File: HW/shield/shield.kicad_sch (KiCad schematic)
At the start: 78 parts, among them J1 TRG, J2 E-STOP, J3 UART, J4 IO, J5 LDP-C BOB, J6 VIN, J7 BREAK, Q1 BSS138, Q2 BSS138, Q3 BSS138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

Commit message: PCB layout
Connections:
- net SCL: now also A1.13 (SDA/A4)
- net SDA: now also A1.14 (SCL/A5)
- no-connect marks 10 -> 8
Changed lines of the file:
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@@
   (junction (at 40.005 72.39) (diameter 0) (color 0 0 0 0)
   )
+  (junction (at 115.57 66.04) (diameter 0) (color 0 0 0 0)
+  )
   (junction (at 38.1 48.26) (diameter 0) (color 0 0 0 0)
   )
@@
   )
   (junction (at 76.2 81.28) (diameter 0) (color 0 0 0 0)
+  )
+  (junction (at 116.205 63.5) (diameter 0) (color 0 0 0 0)
   )
   (no_connect (at 114.935 30.48))
   (no_connect (at 99.695 20.32))
-  (no_connect (at 114.935 55.88))
-  (no_connect (at 114.935 58.42))
   (no_connect (at 44.45 132.08))
   (no_connect (at 114.935 35.56))
@@
     (stroke (width 0) (type default) (color 0 0 0 0))
   )
+  (wire (pts (xy 116.205 63.5) (xy 121.92 63.5))
+    (stroke (width 0) (type default) (color 0 0 0 0))
+  )
   (wire (pts (xy 165.735 66.04) (xy 176.53 66.04))
     (stroke (width 0) (type default) (color 0 0 0 0))
@@
     (stroke (width 0) (type default) (color 0 0 0 0))
   )
+  (wire (pts (xy 115.57 66.04) (xy 133.985 66.04))
+    (stroke (width 0) (type default) (color 0 0 0 0))
+  )
   (wire (pts (xy 165.1 135.255) (xy 156.845 135.255))
     (stroke (width 0) (type default) (color 0 0 0 0))
@@
     (stroke (width 0) (type default) (color 0 0 0 0))
   )
+  (wire (pts (xy 114.935 55.88) (xy 116.205 55.88))
+    (stroke (width 0) (type default) (color 0 0 0 0))
+  )
   (wire (pts (xy 250.19 50.8) (xy 250.19 44.45))
     (stroke (width 0) (type default) (color 0 0 0 0))
@@
     (stroke (width 0) (type default) (color 0 0 0 0))
   )
-  (wire (pts (xy 114.935 66.04) (xy 133.985 66.04))
+  (wire (pts (xy 114.935 66.04) (xy 115.57 66.04))
     (stroke (width 0) (type default) (color 0 0 0 0))
   )
@@
     (stroke (width 0) (type default) (color 0 0 0 0))
   )
-  (wire (pts (xy 114.935 63.5) (xy 121.92 63.5))
+  (wire (pts (xy 114.935 63.5) (xy 116.205 63.5))
     (stroke (width 0) (type default) (color 0 0 0 0))
   )
@@
     (stroke (width 0) (type default) (color 0 0 0 0))
   )
+  (wire (pts (xy 115.57 58.42) (xy 115.57 66.04))
+    (stroke (width 0) (type default) (color 0 0 0 0))
+  )
   (wire (pts (xy 40.005 64.135) (xy 40.005 72.39))
     (stroke (width 0) (type default) (color 0 0 0 0))
@@
     (stroke (width 0) (type default) (color 0 0 0 0))
   )
+  (wire (pts (xy 114.935 58.42) (xy 115.57 58.42))
+    (stroke (width 0) (type default) (color 0 0 0 0))
+  )
   (wire (pts (xy 260.35 36.83) (xy 269.875 36.83))
     (stroke (width 0) (type default) (color 0 0 0 0))
@@
     (stroke (width 0) (type default) (color 0 0 0 0))
   )
+  (wire (pts (xy 116.205 55.88) (xy 116.205 63.5))
+    (stroke (width 0) (type default) (color 0 0 0 0))
+  )

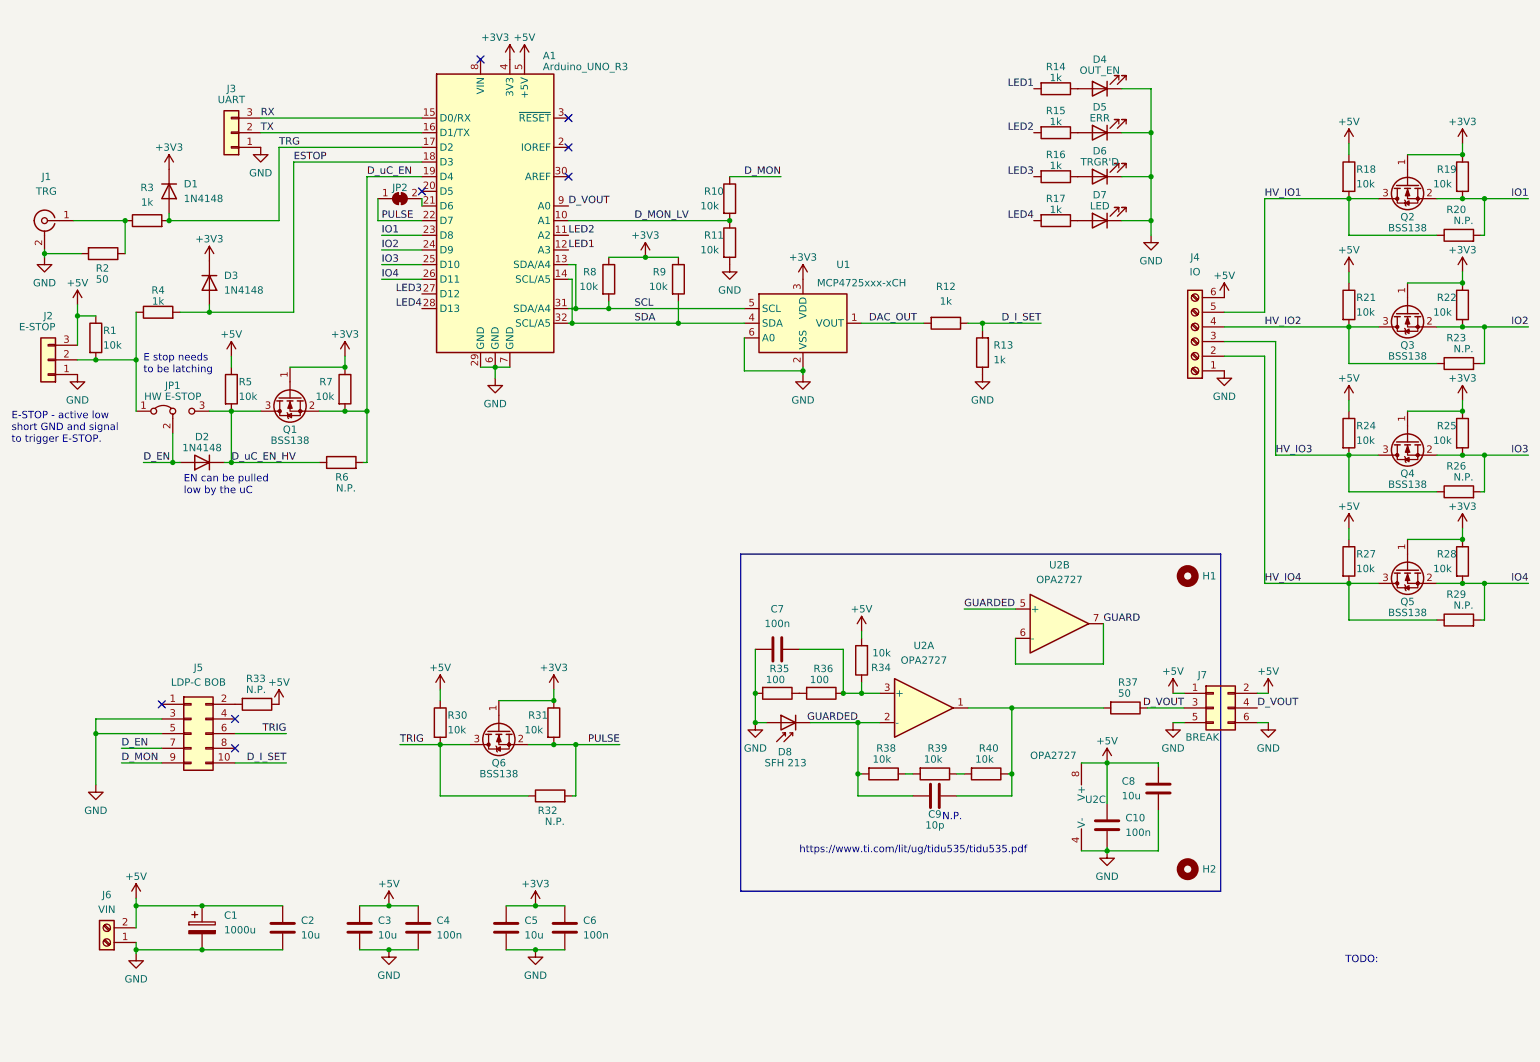
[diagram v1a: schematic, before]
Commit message: PCB routing finished, needs checking
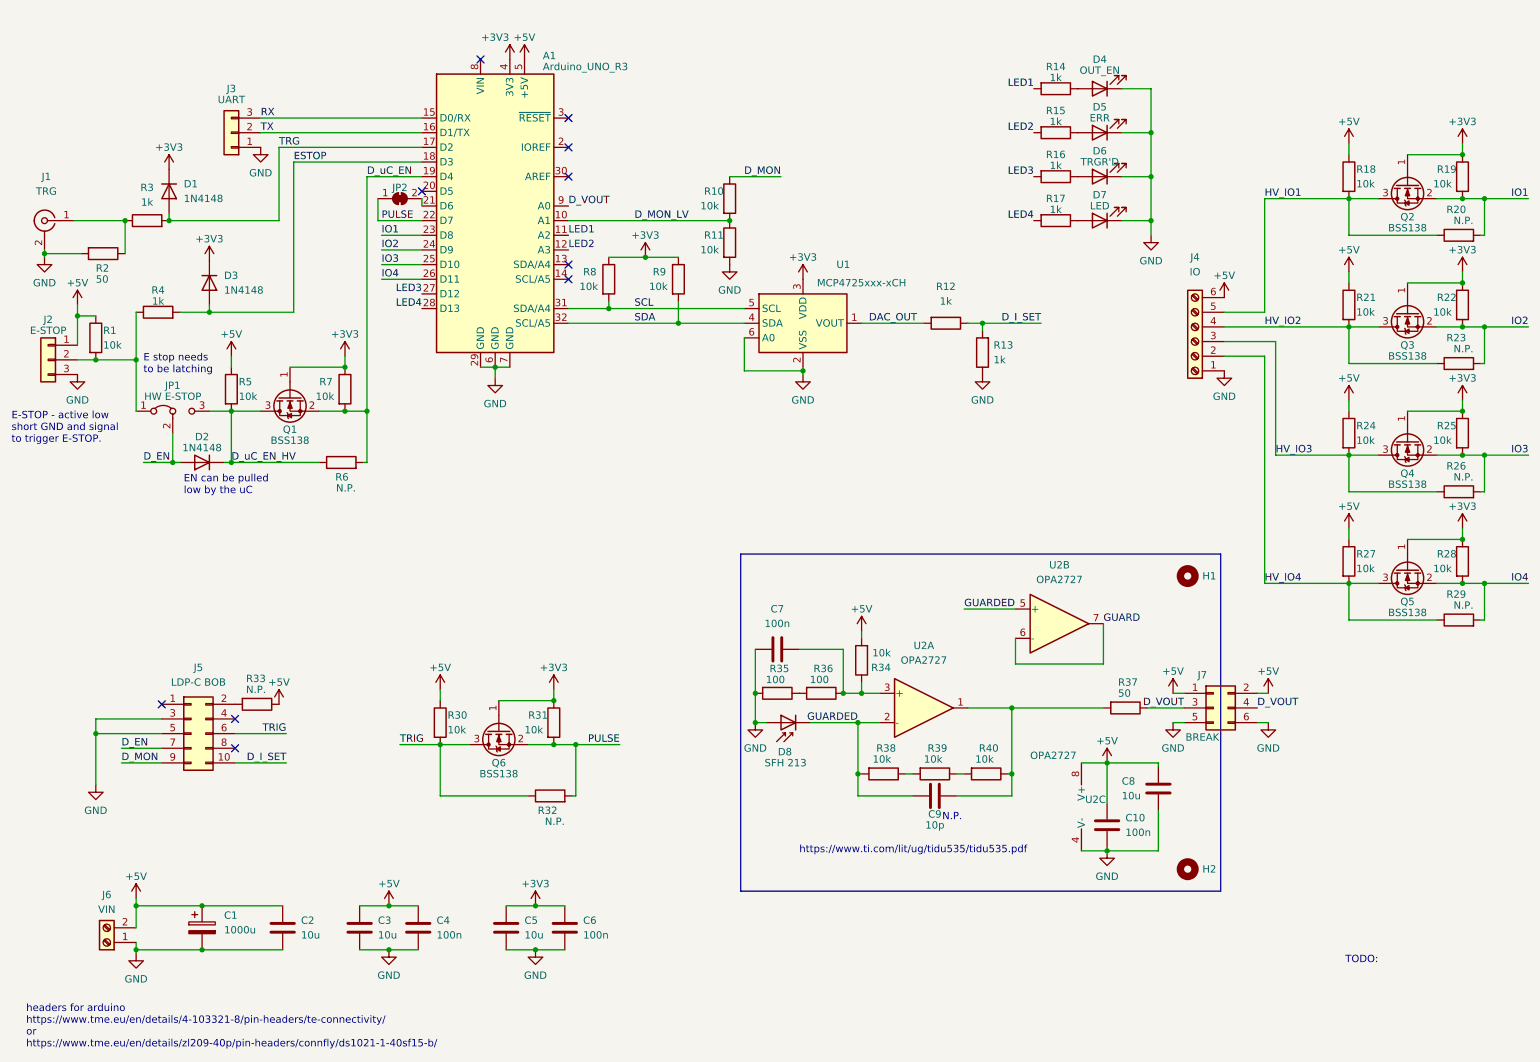
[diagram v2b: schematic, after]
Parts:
- JP2: footprint Jumper:SolderJumper-2_P1.3mm_Open_RoundedPad1.0x1.5mm -> Jumper:SolderJumper-2_P1.3mm_Bridged2Bar_RoundedPad1.0x1.5mm
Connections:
- net +5V: now also J2.1 (Pin_1); no longer J2.3 (Pin_3)
- net GND: now also J2.3 (Pin_3); no longer J2.1 (Pin_1)
- net LED1: now also A1.11 (A2); no longer A1.12 (A3)
- net LED2: now also A1.12 (A3); no longer A1.11 (A2)
- net SCL: no longer A1.13 (SDA/A4)
- net SDA: no longer A1.14 (SCL/A5)
- no-connect marks 8 -> 10
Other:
- note added: "headers for arduino https://www.tme.eu/en/details/4-103321-8/pin-headers/te-connectivity/ or https://www.tme.eu/en/details/zl209-40p/pin-headers/connfly/ds1021-1-40sf15-b/"
- moved on the sheet: J2
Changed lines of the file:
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@@
   (junction (at 40.005 72.39) (diameter 0) (color 0 0 0 0)
   )
-  (junction (at 115.57 66.04) (diameter 0) (color 0 0 0 0)
-  )
   (junction (at 38.1 48.26) (diameter 0) (color 0 0 0 0)
   )
@@
   (junction (at 76.2 81.28) (diameter 0) (color 0 0 0 0)
   )
-  (junction (at 116.205 63.5) (diameter 0) (color 0 0 0 0)
-  )
   (no_connect (at 114.935 30.48))
   (no_connect (at 99.695 20.32))
@@
   (no_connect (at 114.935 40.64))
   (no_connect (at 89.535 43.18))
+  (no_connect (at 114.935 55.88))
   (no_connect (at 57.15 139.7))
   (no_connect (at 57.15 134.62))
+  (no_connect (at 114.935 58.42))
   (wire (pts (xy 51.435 167.005) (xy 65.405 167.005))
     (stroke (width 0) (type default) (color 0 0 0 0))
@@
     (stroke (width 0) (type default) (color 0 0 0 0))
   )
-  (wire (pts (xy 116.205 63.5) (xy 121.92 63.5))
+  (wire (pts (xy 114.935 63.5) (xy 121.92 63.5))
     (stroke (width 0) (type default) (color 0 0 0 0))
   )
@@
     (stroke (width 0) (type default) (color 0 0 0 0))
   )
-  (wire (pts (xy 115.57 66.04) (xy 133.985 66.04))
+  (wire (pts (xy 114.935 66.04) (xy 133.985 66.04))
     (stroke (width 0) (type default) (color 0 0 0 0))
   )
@@
     (stroke (width 0) (type default) (color 0 0 0 0))
   )
-  (wire (pts (xy 114.935 55.88) (xy 116.205 55.88))
-    (stroke (width 0) (type default) (color 0 0 0 0))
-  )
   (wire (pts (xy 250.19 50.8) (xy 250.19 44.45))
     (stroke (width 0) (type default) (color 0 0 0 0))
@@
     (stroke (width 0) (type default) (color 0 0 0 0))
   )
-  (wire (pts (xy 114.935 66.04) (xy 115.57 66.04))
-    (stroke (width 0) (type default) (color 0 0 0 0))
-  )
   (wire (pts (xy 66.675 73.66) (xy 76.2 73.66))
     (stroke (width 0) (type default) (color 0 0 0 0))
@@
     (stroke (width 0) (type default) (color 0 0 0 0))
   )
-  (wire (pts (xy 114.935 63.5) (xy 116.205 63.5))
-    (stroke (width 0) (type default) (color 0 0 0 0))
-  )
   (wire (pts (xy 52.705 62.865) (xy 52.705 64.135))
     (stroke (width 0) (type default) (color 0 0 0 0))
@@
     (stroke (width 0) (type default) (color 0 0 0 0))
   )
-  (wire (pts (xy 115.57 58.42) (xy 115.57 66.04))
-    (stroke (width 0) (type default) (color 0 0 0 0))
-  )
   (wire (pts (xy 40.005 64.135) (xy 40.005 72.39))
     (stroke (width 0) (type default) (color 0 0 0 0))
@@
     (stroke (width 0) (type default) (color 0 0 0 0))
   )
-  (wire (pts (xy 114.935 58.42) (xy 115.57 58.42))
-    (stroke (width 0) (type default) (color 0 0 0 0))
-  )
   (wire (pts (xy 260.35 36.83) (xy 269.875 36.83))
     (stroke (width 0) (type default) (color 0 0 0 0))
@@
     (stroke (width 0) (type default) (color 0 0 0 0))
   )
-  (wire (pts (xy 116.205 55.88) (xy 116.205 63.5))
-    (stroke (width 0) (type default) (color 0 0 0 0))
-  )
   (wire (pts (xy 92.71 129.54) (xy 92.71 131.445))
     (stroke (width 0) (type default) (color 0 0 0 0))
@@
     (effects (font (size 1.27 1.27)) (justify left bottom))
   )
+  (text "headers for arduino\nhttps://www.tme.eu/en/details/4-103321-8/pin-headers/te-connectivity/\nor\nhttps://www.tme.eu/en/details/zl209-40p/pin-headers/connfly/ds1021-1-40sf15-b/"
+    (at 20.955 191.77 0)
+    (effects (font (size 1.27 1.27)) (justify left bottom))
+  )
   (text "N.P." (at 179.705 152.4 0)
     (effects (font (size 1.27 1.27)) (justify left bottom))
@@
     (effects (font (size 1.27 1.27)) (justify left bottom))
   )
-  (label "LED1" (at 114.935 53.34 0)
+  (label "LED1" (at 114.935 50.8 0)
     (effects (font (size 1.27 1.27)) (justify left bottom))
   )
@@
     (effects (font (size 1.27 1.27)) (justify left bottom))
   )
-  (label "LED2" (at 114.935 50.8 0)
+  (label "LED2" (at 114.935 53.34 0)
     (effects (font (size 1.27 1.27)) (justify left bottom))
   )
@@
     (pin "2")
   )
-  (symbol (lib_id "Connector_Generic:Conn_01x03") (at 24.765 72.39 180) (unit 1)
+  (symbol (lib_id "Connector_Generic:Conn_01x03") (at 24.765 72.39 0) (mirror y) (unit 1)
     (in_bom yes) (on_board yes)
-    (property "Reference" "J2" (id 0) (at 24.765 64.77 0))
-    (property "Value" "E-STOP" (id 1) (at 22.86 66.675 0))
+    (property "Reference" "J2" (id 0) (at 24.765 65.405 0))
+    (property "Value" "E-STOP" (id 1) (at 24.765 67.31 0))
     (property "Footprint" "TerminalBlock:TerminalBlock_Altech_AK300-3_P5.00mm" (id 2) (at 24.765 72.39 0)
       (effects (font (size 1.27 1.27)) hide)
@@
       (effects (font (size 1.27 1.27)) hide)
     )
-    (property "Footprint" "Jumper:SolderJumper-2_P1.3mm_Open_RoundedPad1.0x1.5mm" (id 2) (at 85.725 44.45 0)
+    (property "Footprint" "Jumper:SolderJumper-2_P1.3mm_Bridged2Bar_RoundedPad1.0x1.5mm" (id 2) (at 85.725 44.45 0)
       (effects (font (size 1.27 1.27)) hide)
     )
@@
     )
     (path "/69e4916a-fcd5-499c-859e-5b7a7ee48695"
-      (reference "JP2") (unit 1) (value "INTR") (footprint "Jumper:SolderJumper-2_P1.3mm_Open_RoundedPad1.0x1.5mm")
+      (reference "JP2") (unit 1) (value "INTR") (footprint "Jumper:SolderJumper-2_P1.3mm_Bridged2Bar_RoundedPad1.0x1.5mm")
     )
     (path "/6a7a0bfa-65c7-4518-a3bd-a77ff7b676a3"

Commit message: added LDO, BOM
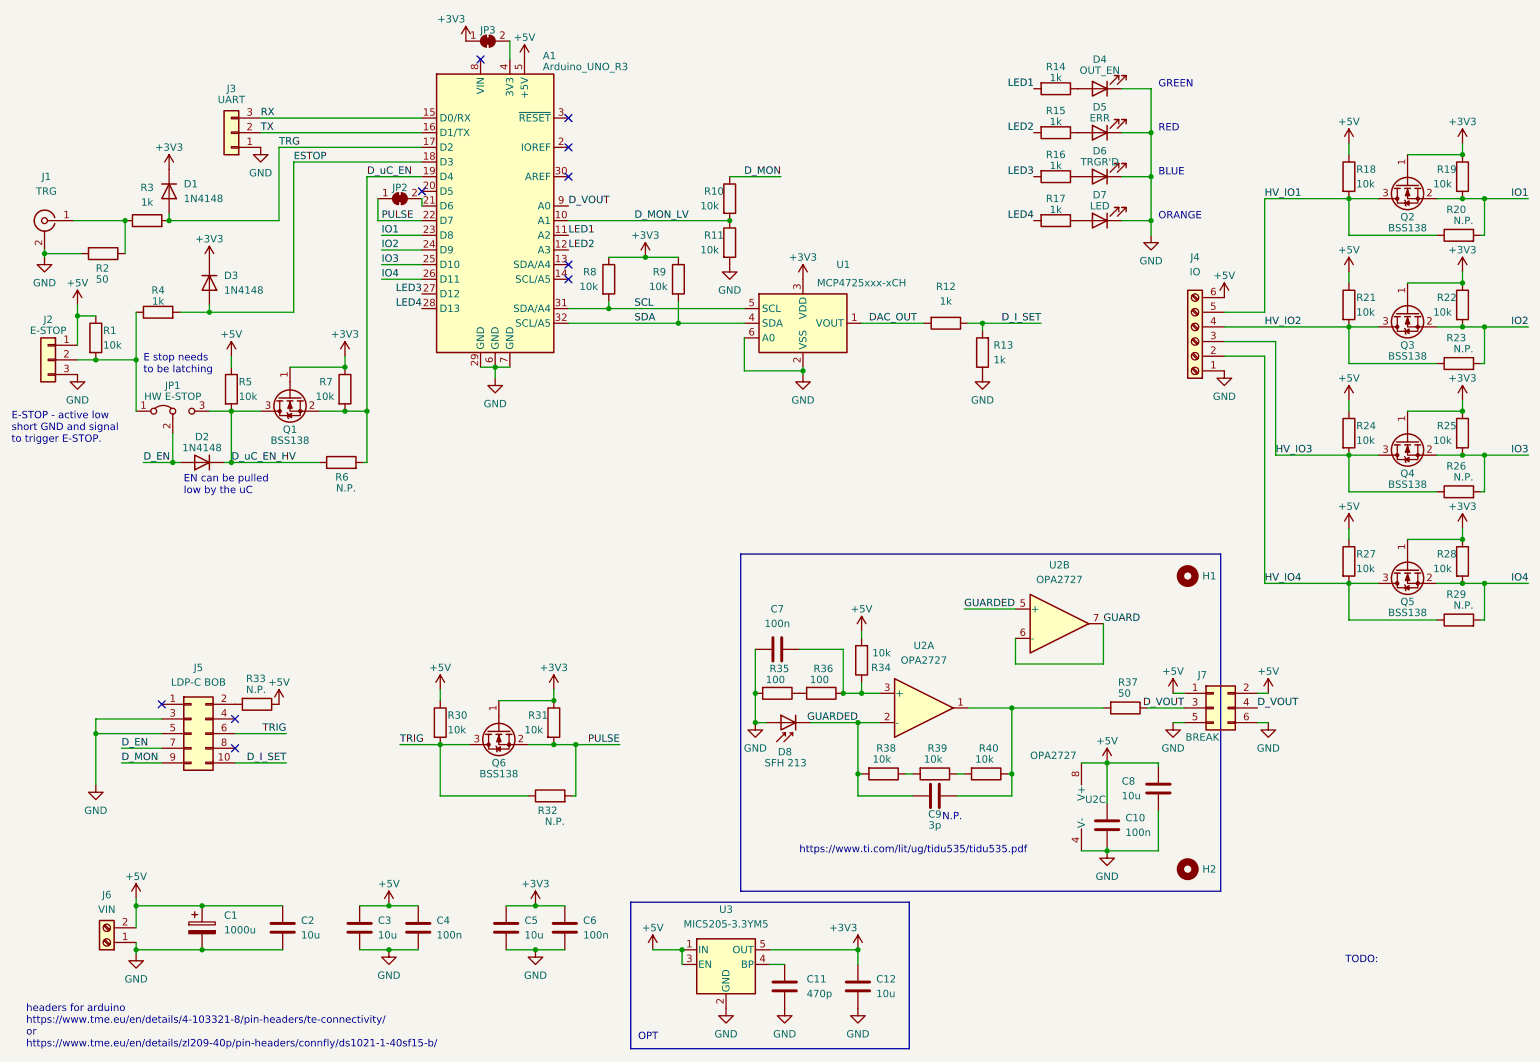
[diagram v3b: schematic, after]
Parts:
- added C11: 470p, Capacitor_SMD:C_0805_2012Metric_Pad1.18x1.45mm_HandSolder, symbol Device:C
- added C12: 10u, Capacitor_SMD:C_0805_2012Metric_Pad1.18x1.45mm_HandSolder, symbol Device:C
- added JP3: INTR, Jumper:SolderJumper-2_P1.3mm_Bridged2Bar_RoundedPad1.0x1.5mm, symbol Jumper:SolderJumper_2_Bridged
- added U3: MIC5205-3.3YM5, Package_TO_SOT_SMD:SOT-23-5, symbol Regulator_Linear:MIC5205-3.3YM5
- C9: value 10p -> 3p
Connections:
- net +3V3: now also C12.1, JP3.1 (A), U3.5 (OUT); no longer A1.4 (3V3)
- net +5V: now also U3.1 (IN), U3.3 (EN)
- net GND: now also C11.1, C12.2, U3.2 (GND)
- new net: C11.2, U3.4 (BP)
- new net: A1.4 (3V3), JP3.2 (B)
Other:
- note added: "BLUE"
- note added: "GREEN"
- note added: "OPT"
- note added: "ORANGE"
- note added: "RED"
